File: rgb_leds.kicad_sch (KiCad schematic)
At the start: 12 parts

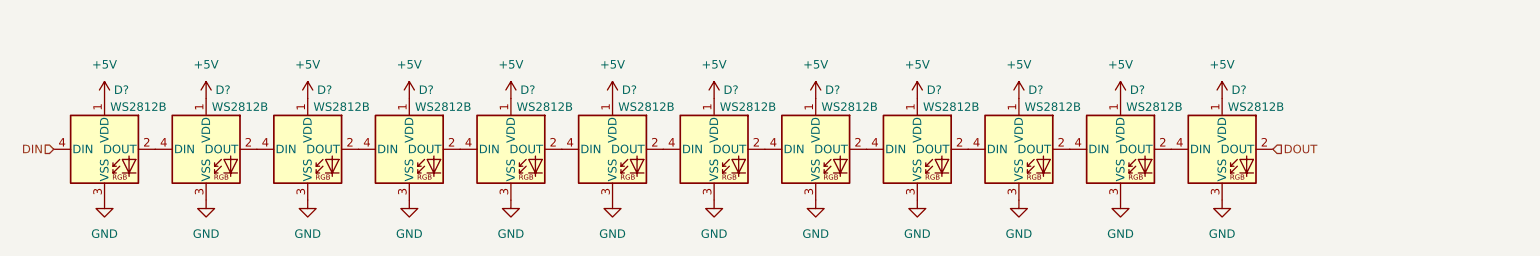
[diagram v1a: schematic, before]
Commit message: added audio ref schematic, added bat to 5V, added shift register, connected devices with other periferals
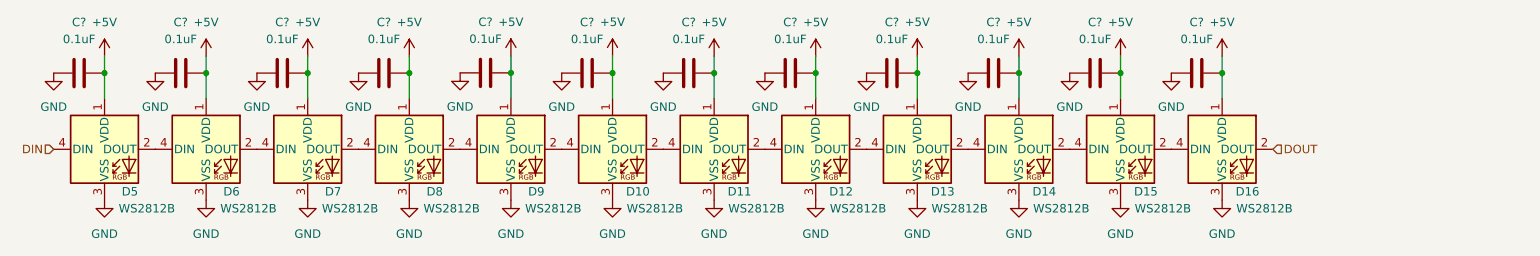
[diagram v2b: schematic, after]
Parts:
- added C? (x12): 0.1uF, symbol Device:C
- gave numbers to parts that had none: 12
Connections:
- net +5V: now also C?.2, C?.2, C?.2, C?.2, C?.2, C?.2, C?.2, C?.2, C?.2, C?.2, C?.2, C?.2; no longer D9.1 (VDD)
- net GND: now also C?.1, C?.1, C?.1, C?.1, C?.1, C?.1, C?.1, C?.1, C?.1, C?.1, C?.1, C?.1

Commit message: added adcin2 config description, fixed some rule check errors
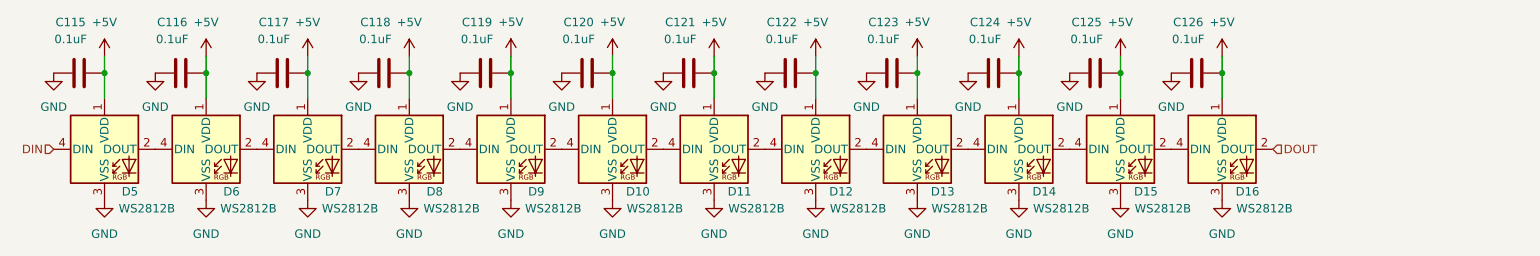
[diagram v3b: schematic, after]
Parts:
- gave numbers to parts that had none: 12
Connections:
- net +5V: now also D9.1 (VDD)

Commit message: minor optimized pinassignement, added capacitors, added connectors
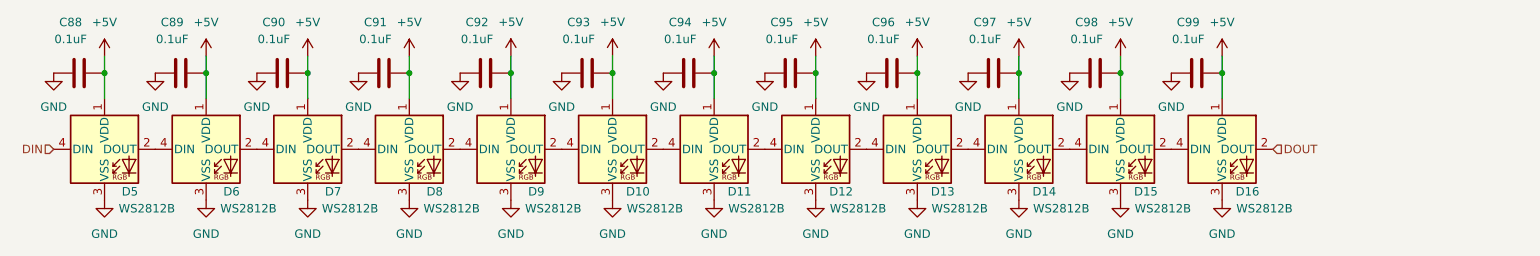
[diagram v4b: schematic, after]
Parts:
- renumbered C115 to C88, C116 to C89, C117 to C90, C118 to C91, C119 to C92, C120 to C93, C121 to C94, C122 to C95, C123 to C96, C124 to C97, C125 to C98, C126 to C99

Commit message: PI LC lowpass filter, added CP2012 reset, added connectors
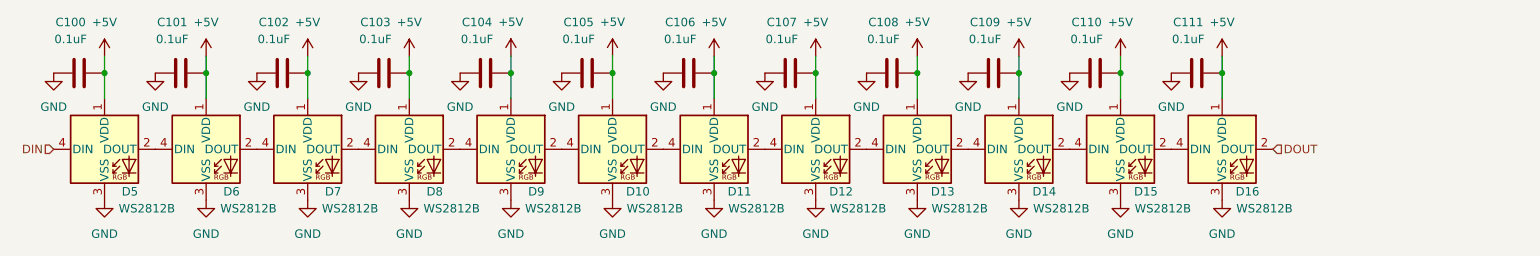
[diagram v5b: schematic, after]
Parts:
- renumbered C88 to C100, C89 to C101, C90 to C102, C91 to C103, C92 to C104, C93 to C105, C94 to C106, C95 to C107, C96 to C108, C97 to C109, C98 to C110, C99 to C111

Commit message: datasheet checkout, added couple of capacitors for usb-c, groupd some scheatics
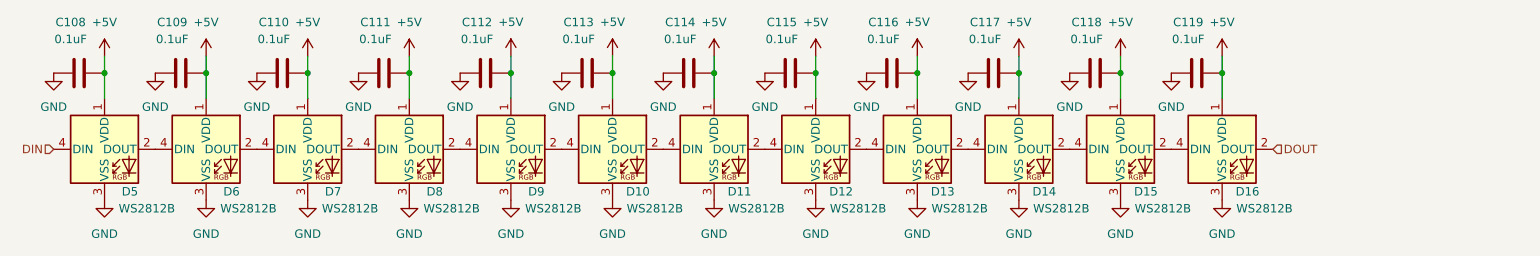
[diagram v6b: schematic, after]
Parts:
- renumbered C100 to C108, C101 to C109, C102 to C110, C103 to C111, C104 to C112, C105 to C113, C106 to C114, C107 to C115, C108 to C116, C109 to C117, C110 to C118, C111 to C119

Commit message: added nfc antenna components, added most of footprints
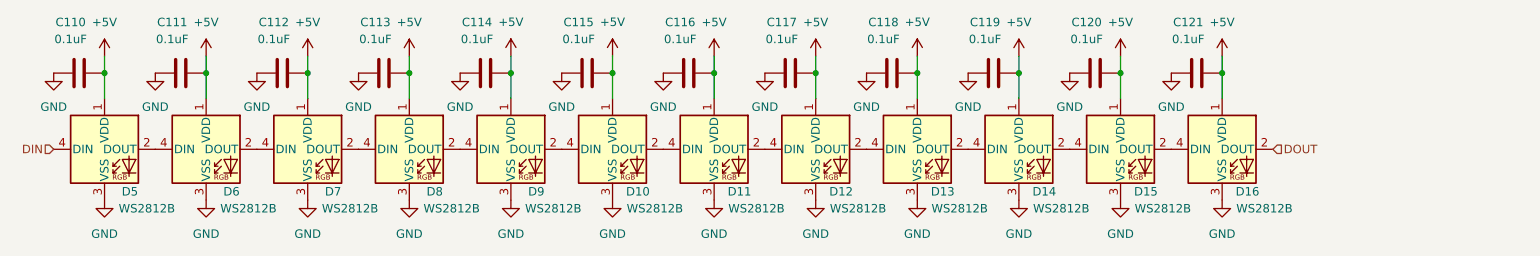
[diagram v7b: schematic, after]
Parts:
- C110: renamed from C108; footprint (none) -> Capacitor_SMD:C_0603_1608Metric_Pad1.08x0.95mm_HandSolder
- C111: renamed from C109; footprint (none) -> Capacitor_SMD:C_0603_1608Metric_Pad1.08x0.95mm_HandSolder
- C112: renamed from C110; footprint (none) -> Capacitor_SMD:C_0603_1608Metric_Pad1.08x0.95mm_HandSolder
- C113: renamed from C111; footprint (none) -> Capacitor_SMD:C_0603_1608Metric_Pad1.08x0.95mm_HandSolder
- C114: renamed from C112; footprint (none) -> Capacitor_SMD:C_0603_1608Metric_Pad1.08x0.95mm_HandSolder
- C115: renamed from C113; footprint (none) -> Capacitor_SMD:C_0603_1608Metric_Pad1.08x0.95mm_HandSolder
- C116: renamed from C114; footprint (none) -> Capacitor_SMD:C_0603_1608Metric_Pad1.08x0.95mm_HandSolder
- C117: renamed from C115; footprint (none) -> Capacitor_SMD:C_0603_1608Metric_Pad1.08x0.95mm_HandSolder
- C118: renamed from C116; footprint (none) -> Capacitor_SMD:C_0603_1608Metric_Pad1.08x0.95mm_HandSolder
- C119: renamed from C117; footprint (none) -> Capacitor_SMD:C_0603_1608Metric_Pad1.08x0.95mm_HandSolder
- C120: renamed from C118; footprint (none) -> Capacitor_SMD:C_0603_1608Metric_Pad1.08x0.95mm_HandSolder
- C121: renamed from C119; footprint (none) -> Capacitor_SMD:C_0603_1608Metric_Pad1.08x0.95mm_HandSolder
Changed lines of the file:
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@@
   (symbol (lib_id "Device:C") (at 207.01 76.2 90) (unit 1)
     (in_bom yes) (on_board yes)
-    (property "Reference" "C118" (id 0) (at 205.74 68.58 90))
+    (property "Reference" "C120" (id 0) (at 205.74 68.58 90))
     (property "Value" "0.1uF" (id 1) (at 205.74 71.12 90))
-    (property "Footprint" "" (id 2) (at 210.82 75.2348 0)
+    (property "Footprint" "Capacitor_SMD:C_0603_1608Metric_Pad1.08x0.95mm_HandSolder" (id 2) (at 210.82 75.2348 0)
       (effects (font (size 1.27 1.27)) hide)
     )
@@
   (symbol (lib_id "Device:C") (at 191.77 76.2 90) (unit 1)
     (in_bom yes) (on_board yes)
-    (property "Reference" "C117" (id 0) (at 190.5 68.58 90))
+    (property "Reference" "C119" (id 0) (at 190.5 68.58 90))
     (property "Value" "0.1uF" (id 1) (at 190.5 71.12 90))
-    (property "Footprint" "" (id 2) (at 195.58 75.2348 0)
+    (property "Footprint" "Capacitor_SMD:C_0603_1608Metric_Pad1.08x0.95mm_HandSolder" (id 2) (at 195.58 75.2348 0)
       (effects (font (size 1.27 1.27)) hide)
     )
@@
   (symbol (lib_id "Device:C") (at 222.25 76.2 90) (unit 1)
     (in_bom yes) (on_board yes)
-    (property "Reference" "C119" (id 0) (at 220.98 68.58 90))
+    (property "Reference" "C121" (id 0) (at 220.98 68.58 90))
     (property "Value" "0.1uF" (id 1) (at 220.98 71.12 90))
-    (property "Footprint" "" (id 2) (at 226.06 75.2348 0)
+    (property "Footprint" "Capacitor_SMD:C_0603_1608Metric_Pad1.08x0.95mm_HandSolder" (id 2) (at 226.06 75.2348 0)
       (effects (font (size 1.27 1.27)) hide)
     )
@@
   (symbol (lib_id "Device:C") (at 130.81 76.2 90) (unit 1)
     (in_bom yes) (on_board yes)
-    (property "Reference" "C113" (id 0) (at 129.54 68.58 90))
+    (property "Reference" "C115" (id 0) (at 129.54 68.58 90))
     (property "Value" "0.1uF" (id 1) (at 129.54 71.12 90))
-    (property "Footprint" "" (id 2) (at 134.62 75.2348 0)
+    (property "Footprint" "Capacitor_SMD:C_0603_1608Metric_Pad1.08x0.95mm_HandSolder" (id 2) (at 134.62 75.2348 0)
       (effects (font (size 1.27 1.27)) hide)
     )
@@
   (symbol (lib_id "Device:C") (at 69.85 76.2 90) (unit 1)
     (in_bom yes) (on_board yes)
-    (property "Reference" "C109" (id 0) (at 68.58 68.58 90))
+    (property "Reference" "C111" (id 0) (at 68.58 68.58 90))
     (property "Value" "0.1uF" (id 1) (at 68.58 71.12 90))
-    (property "Footprint" "" (id 2) (at 73.66 75.2348 0)
+    (property "Footprint" "Capacitor_SMD:C_0603_1608Metric_Pad1.08x0.95mm_HandSolder" (id 2) (at 73.66 75.2348 0)
       (effects (font (size 1.27 1.27)) hide)
     )
@@
   (symbol (lib_id "Device:C") (at 161.29 76.2 90) (unit 1)
     (in_bom yes) (on_board yes)
-    (property "Reference" "C115" (id 0) (at 160.02 68.58 90))
+    (property "Reference" "C117" (id 0) (at 160.02 68.58 90))
     (property "Value" "0.1uF" (id 1) (at 160.02 71.12 90))
-    (property "Footprint" "" (id 2) (at 165.1 75.2348 0)
+    (property "Footprint" "Capacitor_SMD:C_0603_1608Metric_Pad1.08x0.95mm_HandSolder" (id 2) (at 165.1 75.2348 0)
       (effects (font (size 1.27 1.27)) hide)
     )
@@
   (symbol (lib_id "Device:C") (at 100.33 76.2 90) (unit 1)
     (in_bom yes) (on_board yes)
-    (property "Reference" "C111" (id 0) (at 99.06 68.58 90))
+    (property "Reference" "C113" (id 0) (at 99.06 68.58 90))
     (property "Value" "0.1uF" (id 1) (at 99.06 71.12 90))
-    (property "Footprint" "" (id 2) (at 104.14 75.2348 0)
+    (property "Footprint" "Capacitor_SMD:C_0603_1608Metric_Pad1.08x0.95mm_HandSolder" (id 2) (at 104.14 75.2348 0)
       (effects (font (size 1.27 1.27)) hide)
     )
@@
   (symbol (lib_id "Device:C") (at 85.09 76.2 90) (unit 1)
     (in_bom yes) (on_board yes)
-    (property "Reference" "C110" (id 0) (at 83.82 68.58 90))
+    (property "Reference" "C112" (id 0) (at 83.82 68.58 90))
     (property "Value" "0.1uF" (id 1) (at 83.82 71.12 90))
-    (property "Footprint" "" (id 2) (at 88.9 75.2348 0)
+    (property "Footprint" "Capacitor_SMD:C_0603_1608Metric_Pad1.08x0.95mm_HandSolder" (id 2) (at 88.9 75.2348 0)
       (effects (font (size 1.27 1.27)) hide)
     )
@@
   (symbol (lib_id "Device:C") (at 176.53 76.2 90) (unit 1)
     (in_bom yes) (on_board yes)
-    (property "Reference" "C116" (id 0) (at 175.26 68.58 90))
+    (property "Reference" "C118" (id 0) (at 175.26 68.58 90))
     (property "Value" "0.1uF" (id 1) (at 175.26 71.12 90))
-    (property "Footprint" "" (id 2) (at 180.34 75.2348 0)
+    (property "Footprint" "Capacitor_SMD:C_0603_1608Metric_Pad1.08x0.95mm_HandSolder" (id 2) (at 180.34 75.2348 0)
       (effects (font (size 1.27 1.27)) hide)
     )
@@
   (symbol (lib_id "Device:C") (at 146.05 76.2 90) (unit 1)
     (in_bom yes) (on_board yes)
-    (property "Reference" "C114" (id 0) (at 144.78 68.58 90))
+    (property "Reference" "C116" (id 0) (at 144.78 68.58 90))
     (property "Value" "0.1uF" (id 1) (at 144.78 71.12 90))
-    (property "Footprint" "" (id 2) (at 149.86 75.2348 0)
+    (property "Footprint" "Capacitor_SMD:C_0603_1608Metric_Pad1.08x0.95mm_HandSolder" (id 2) (at 149.86 75.2348 0)
       (effects (font (size 1.27 1.27)) hide)
     )
@@
   (symbol (lib_id "Device:C") (at 54.61 76.2 90) (unit 1)
     (in_bom yes) (on_board yes)
-    (property "Reference" "C108" (id 0) (at 53.34 68.58 90))
+    (property "Reference" "C110" (id 0) (at 53.34 68.58 90))
     (property "Value" "0.1uF" (id 1) (at 53.34 71.12 90))
-    (property "Footprint" "" (id 2) (at 58.42 75.2348 0)
+    (property "Footprint" "Capacitor_SMD:C_0603_1608Metric_Pad1.08x0.95mm_HandSolder" (id 2) (at 58.42 75.2348 0)
       (effects (font (size 1.27 1.27)) hide)
     )
@@
   (symbol (lib_id "Device:C") (at 115.57 76.2 90) (unit 1)
     (in_bom yes) (on_board yes)
-    (property "Reference" "C112" (id 0) (at 114.3 68.58 90))
+    (property "Reference" "C114" (id 0) (at 114.3 68.58 90))
     (property "Value" "0.1uF" (id 1) (at 114.3 71.12 90))
-    (property "Footprint" "" (id 2) (at 119.38 75.2348 0)
-      (effects (font (size 1.27 1.27)) hide)
-    )
+    (property "Footprint" "Capacitor_SMD:C_0603_1608Metric_Pad1.08x0.95mm_HandSolder" (id 2) (at 119.38 75.2348 0)
+      (effects (font (size 1.27 1.27)) hide)
+    )

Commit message: schematic creation
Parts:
- added C128, C129: 0.1uF, Capacitor_SMD:C_0603_1608Metric_Pad1.08x0.95mm_HandSolder, symbol Device:C
- added D17, D18: WS2812B, LED_SMD:LED_WS2812B_PLCC4_5.0x5.0mm_P3.2mm, symbol LED:WS2812B
- renumbered C110 to C116, C111 to C117, C112 to C118, C113 to C119, C114 to C120, C115 to C121, C116 to C122, C117 to C123, C118 to C124, C119 to C125, C120 to C126, C121 to C127
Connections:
- net +5V: now also C129.2, D18.1 (VDD)
- net DOUT: now also D18.2 (DOUT); no longer D16.2 (DOUT)
- net GND: now also C128.1, C129.1, D17.3 (VSS), D18.3 (VSS)
- new net: D17.2 (DOUT), D18.4 (DIN)
- new net: D16.2 (DOUT), D17.4 (DIN)
